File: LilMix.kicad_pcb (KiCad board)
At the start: 2 copper layers, 47 parts, among them J1_L1 PJ301BM, J1_R1 PJ301BM, J2_L1 PJ301BM, J2_R1 PJ301BM, J3 JACK-STEREO-MINI, J4 PJ301BM, J5 PJ301BM, J6 JACK-STEREO-MINI, U1 TL074, U2 NE5532

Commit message: Very rough component placement
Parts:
- moved U1 96.0 mm to (318.4, 112.0), turned to 90 degrees
- moved R1 90.6 mm to (272.6, 121.2)
- moved C1 89.8 mm to (281.6, 122.7)
- moved R15 89.8 mm to (276.8, 122.0)
- moved C10 89.2 mm to (259.6, 122.2)
- moved C9 89.2 mm to (264.4, 122.6)
- moved D1 89.2 mm to (265.9, 119.4)
- moved D2 89.2 mm to (260.1, 119.1)
- moved U2 89.2 mm to (253.0, 120.6)
- moved R5 86.8 mm to (301.4, 111.2)
- moved C3 83.6 mm to (306.2, 110.6)
- moved C4 78.6 mm to (306.8, 121.2)
- moved R17 78.6 mm to (306.9, 116.9)
- moved R9 78.3 mm to (286.1, 122.4)
- moved R6 76.4 mm to (302.6, 117.2)
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
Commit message: Updated rough placement and circuit updates
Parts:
- added JP2: 2x4 Socket, 4ms-footprints:Socket_2x4_2.54mm_TH, F.Cu at (98.9, 145.1)
- added JP3: 2x4 Socket, 4ms-footprints:Socket_2x4_2.54mm_TH, F.Cu at (115.7, 78.9)
- added RV5: 100k, 4ms-footprints:Audio_Mod_Header_1x03, B.Cu at (176.0, 24.9)
- added RV6: 100k, 4ms-footprints:Audio_Mod_Header_1x03, B.Cu at (203.6, 50.6)
- C1, C10, C2, C3, C4, C5, C6, C7, C8, C9, D1, D2, R1, R10, R11, R12, R13, R14, R15, R16, R17, R18, R19, R2, R20, R4, R5, R9, U1, U2: moved to B.Cu
- JP1: value EURO_HEADER_10pin -> 2x8 Power; moved to B.Cu
- R3, R6: value 100k -> 47k; moved to B.Cu
- R7, R8: value 39k -> 100k; moved to B.Cu
- moved J6 232.9 mm to (102.2, 94.5), turned to 270 degrees
- moved RV4 225.0 mm to (99.9, 77.3)
- moved U1 204.2 mm to (115.0, 94.2), turned to 270 degrees
- moved R9 189.0 mm to (103.5, 73.5), turned to 180 degrees
- moved J5 186.8 mm to (146.9, 94.5), turned to 270 degrees
- moved C4 184.6 mm to (123.4, 100.6)
- moved C3 183.1 mm to (124.6, 87.6)
- moved R10 180.1 mm to (97.8, 91.5), turned to 180 degrees
- moved R13 176.9 mm to (120.1, 87.6)
- moved R17 176.8 mm to (131.1, 98.9), turned to 270 degrees
- moved C5 171.3 mm to (114.4, 100.7)
- moved R14 164.9 mm to (128.7, 94.0), turned to 270 degrees
- moved RV1 162.8 mm to (124.0, 77.3)
- moved R7 162.8 mm to (162.3, 19.1)
- moved RV2 159.2 mm to (141.4, 77.3)
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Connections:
- J1_L1 pad 1: GND -> GND_B
- J1_R1 pad 1: GND -> GND_B
- J1_R1 pad 3: Net-(J1_R1-Pad3) -> J1_R_B
- J2_L1 pad 1: GND -> GND_B
- J2_R1 pad 1: GND -> GND_B
- J2_R1 pad 3: Net-(J2_R1-Pad3) -> J2_R_B
- J3 pad 1: J3_INSERT -> J3_L_B
- J3 pad 2: GND -> GND_B
- J3 pad 3: Net-(J3-Pad3) -> J3_R_B
- JP1 pad 1: Net-(JP1-Pad1) -> Net-(D1-Pad2)
- JP1 pad 9: Net-(JP1-Pad9) -> Net-(D2-Pad1)
- R11 pad 2: L_INV -> Net-(R11-Pad2)
- R12 pad 2: R_INV -> Net-(R12-Pad2)
- RV1 pad 3: J1_INSERT -> J1_L_A
- RV1 pad 6: J2_INSERT -> J2_L_A
- RV2 pad 3: J3_INSERT -> J3_L_A
- RV2 pad 6: Net-(J1_R1-Pad3) -> J1_R_A
- RV3 pad 3: Net-(J2_R1-Pad3) -> J2_R_A
- RV3 pad 6: Net-(J3-Pad3) -> J3_R_A
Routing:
- added copper zone on B.Cu, net GND
- added copper zone on F.Cu, net GND
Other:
- board outline added: 46.6 x 1.9 mm
- board text added: "Front 4.8 x 8.1 cm"
- board text added: "Top Drills 2.1 x 8.1 cm"

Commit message: Rought placement complete
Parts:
- J1_L1, J1_R1, J2_L1, J2_R1, J4, J5: value PJ301BM -> MONO
- J3, J6: value JACK-STEREO-MINI -> STEREO
- moved R11 91.2 mm to (115.2, 101.7), turned to 270 degrees
- moved R15 88.8 mm to (118.0, 101.7), turned to 90 degrees
- moved C6 86.2 mm to (111.7, 85.6), turned to 90 degrees
- moved R7 85.7 mm to (108.3, 85.6), turned to 90 degrees
- moved C9 85.1 mm to (120.6, 101.7), turned to 270 degrees
- moved R8 82.0 mm to (118.6, 85.5), turned to 270 degrees
- moved C7 81.7 mm to (122.3, 85.5), turned to 270 degrees
- moved R12 68.0 mm to (151.2, 99.2), turned to 90 degrees
- moved RV5 67.8 mm to (146.9, 86.1), turned to 90 degrees
- moved RV6 64.5 mm to (155.1, 93.2)
- moved C10 62.5 mm to (142.6, 94.7), turned to 90 degrees
- moved R16 61.5 mm to (154.8, 99.3), turned to 270 degrees
- moved R13 6.19 mm to (125.9, 85.5), turned to 90 degrees
- moved C3 5.23 mm to (129.4, 85.6), turned to 270 degrees
- moved R19 3.96 mm to (105.0, 85.6), turned to 90 degrees
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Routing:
- removed copper zone on B.Cu, net GND
- removed copper zone on F.Cu, net GND

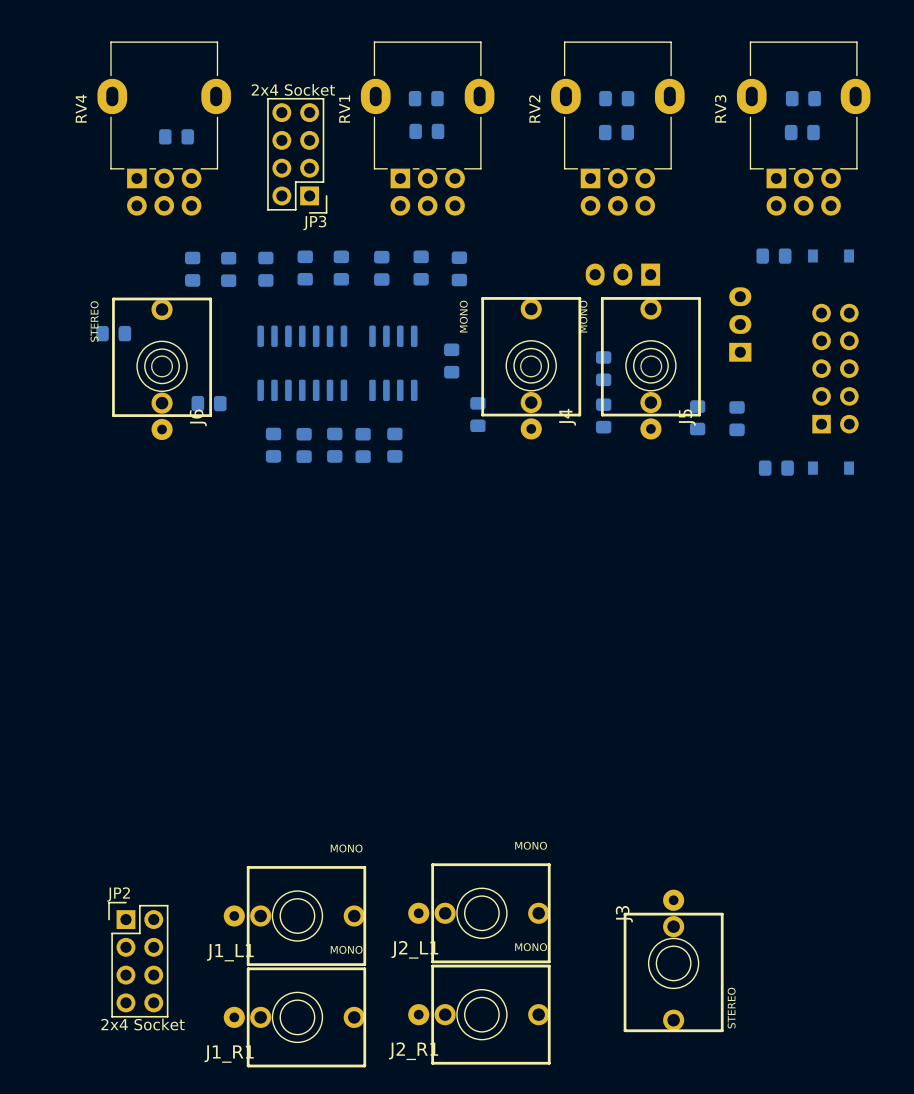
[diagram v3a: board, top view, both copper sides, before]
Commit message: Updated project traces. Added board cuts
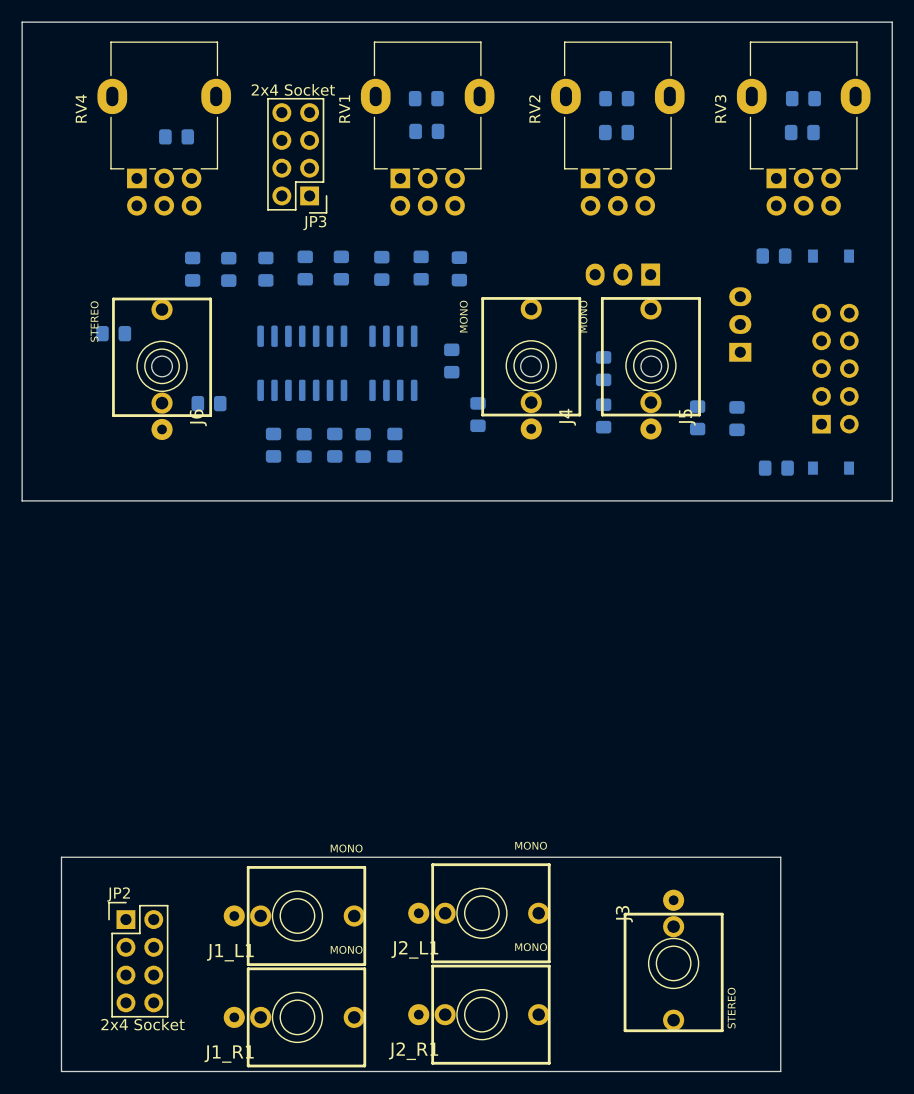
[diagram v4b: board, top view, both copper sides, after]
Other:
- board size 46.6 x 1.9 mm -> 79.6 x 96 mm
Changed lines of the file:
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@@
   (general
     (thickness 1.6)
-    (drawings 11)
+    (drawings 19)
     (tracks 0)
     (zones 0)
@@
   (setup
     (last_trace_width 0.25)
+    (user_trace_width 0.3)
+    (user_trace_width 0.4)
+    (user_trace_width 0.5)
+    (user_trace_width 0.75)
     (trace_clearance 0.2)
     (zone_clearance 0.508)
@@
     )
   )
+  (gr_line (start 169 106.8) (end 89.4 106.8) (layer Edge.Cuts) (width 0.05))
+  (gr_line (start 89.4 63) (end 89.4 106.8) (layer Edge.Cuts) (width 0.05))
+  (gr_line (start 169 63) (end 89.4 63) (layer Edge.Cuts) (width 0.05))
+  (gr_line (start 169 106.8) (end 169 63) (layer Edge.Cuts) (width 0.05))
+  (gr_line (start 93 139.4) (end 93 159) (layer Edge.Cuts) (width 0.05))
+  (gr_line (start 158.8 139.4) (end 93 139.4) (layer Edge.Cuts) (width 0.05))
+  (gr_line (start 158.8 159) (end 158.8 139.4) (layer Edge.Cuts) (width 0.05))
+  (gr_line (start 93 159) (end 158.8 159) (layer Edge.Cuts) (width 0.05))
   (gr_circle (center 146.956602 94.5) (end 147.756602 94) (layer Edge.Cuts) (width 0.05))
   (gr_circle (center 135.956602 94.5) (end 136.756602 94) (layer Edge.Cuts) (width 0.05))

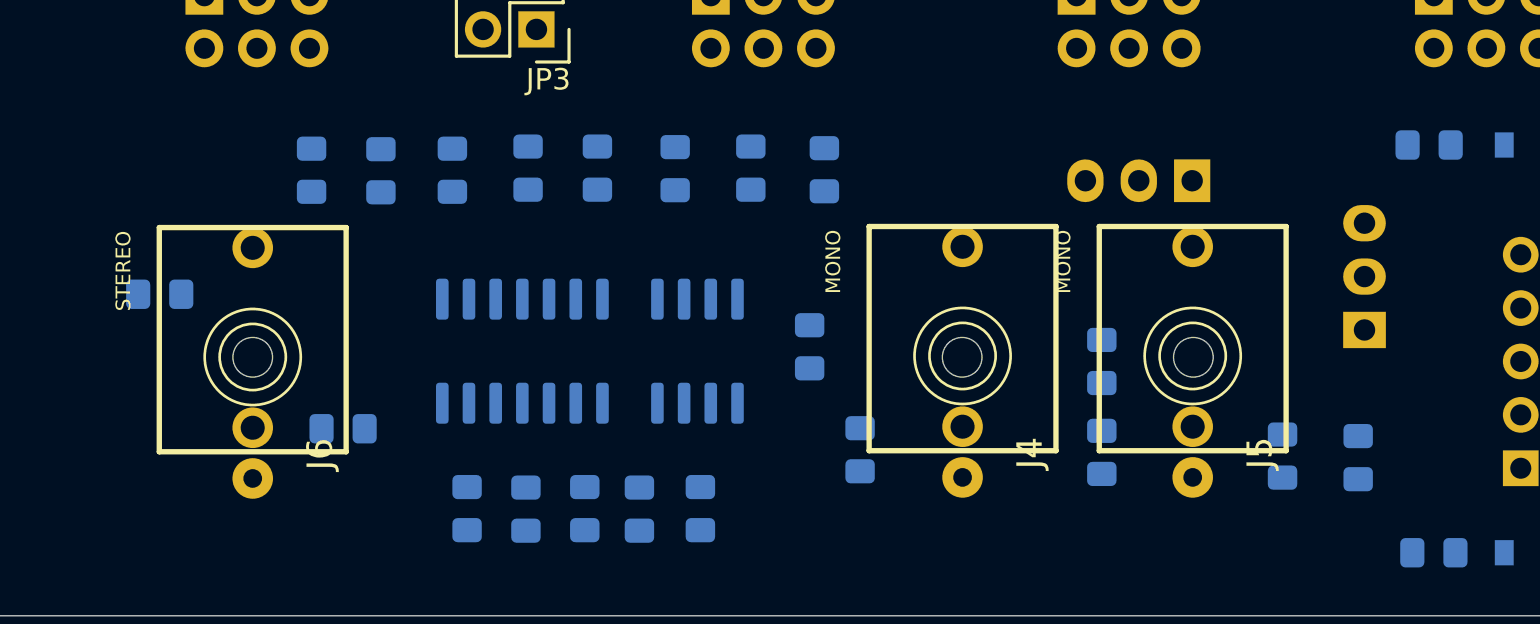
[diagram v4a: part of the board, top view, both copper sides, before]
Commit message: Added power sockets for other modules
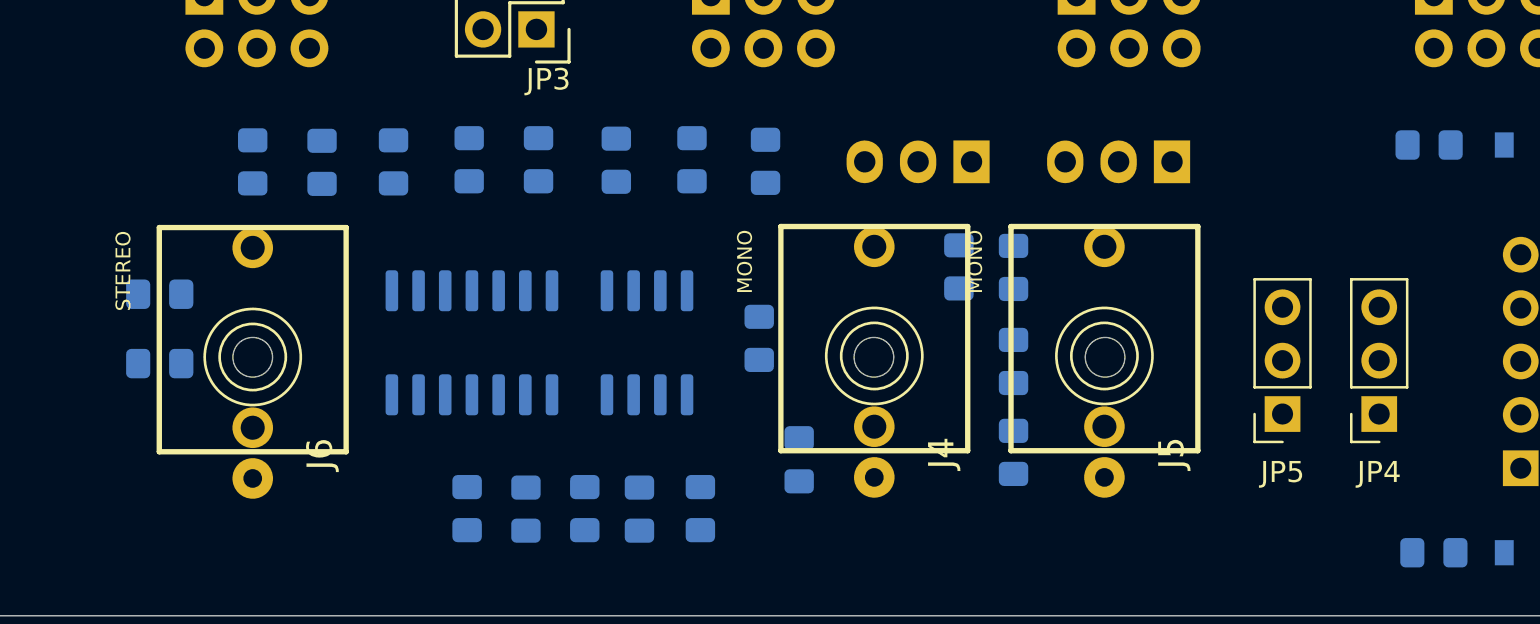
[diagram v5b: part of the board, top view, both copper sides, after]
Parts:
- added JP4: Conn_01x03, Connector_PinSocket_2.54mm:PinSocket_1x03_P2.54mm_Vertical, F.Cu at (155.8, 97.2)
- added JP5: Conn_01x03, Connector_PinSocket_2.54mm:PinSocket_1x03_P2.54mm_Vertical, F.Cu at (151.2, 97.2)
- moved R16 21.1 mm to (135.8, 90.2), turned to 90 degrees
- moved R12 15.6 mm to (138.4, 90.2)
- moved RV6 12.2 mm to (145.9, 85.2), turned to 90 degrees
- moved RV5 10.5 mm to (136.4, 85.2)
- moved R20 9.26 mm to (97.8, 94.8)
- moved J5 4.20 mm to (142.7, 94.5)
- moved C10 4.20 mm to (138.4, 94.7)
- moved J4 4.20 mm to (131.8, 94.5)
- moved R18 4.20 mm to (138.4, 99.0)
- moved R17 2.94 mm to (128.2, 99.4)
- moved C3 2.83 mm to (126.6, 85.2)
- moved R13 2.83 mm to (123.1, 85.1)
- moved C7 2.83 mm to (119.5, 85.1)
- moved C8 2.83 mm to (112.5, 85.1)
- moved R7 2.83 mm to (105.5, 85.2)
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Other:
- outline, holes or cut-outs redrawn

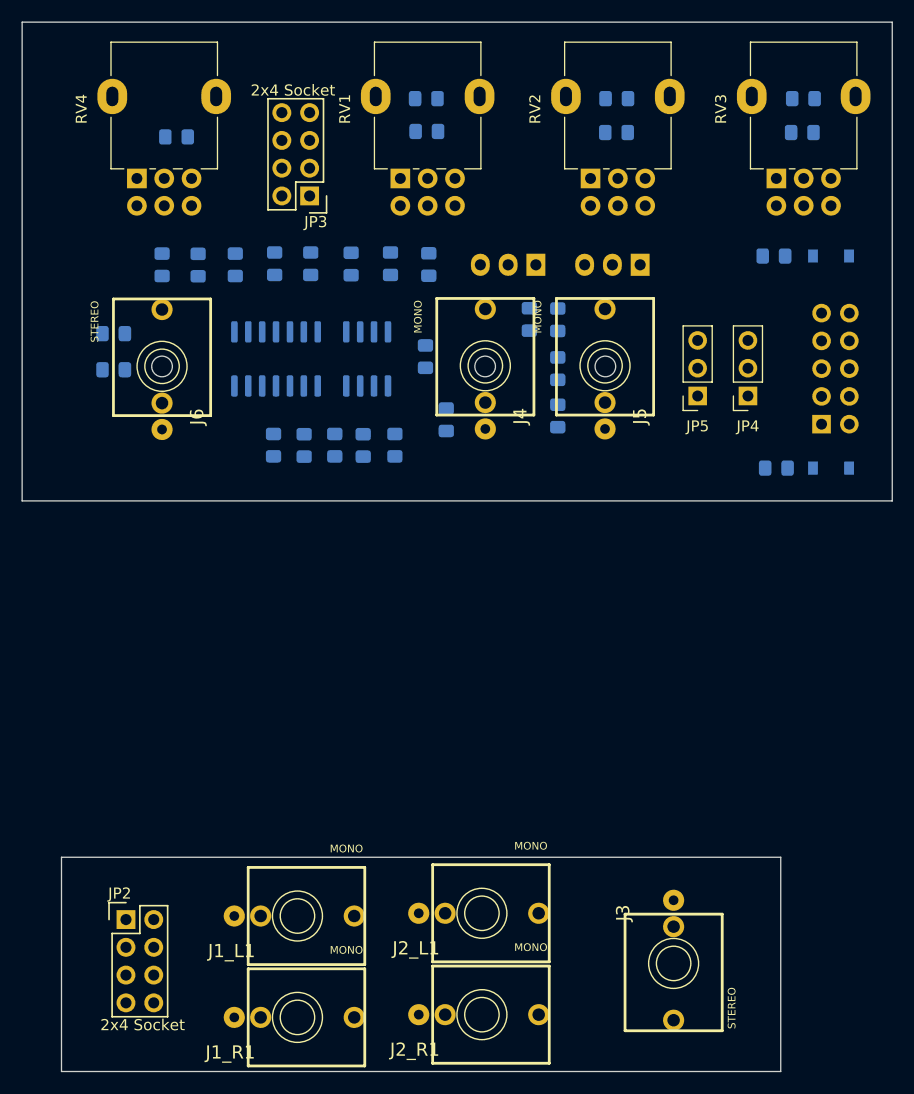
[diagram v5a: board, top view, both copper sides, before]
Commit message: Updated footprint of stereo jacks
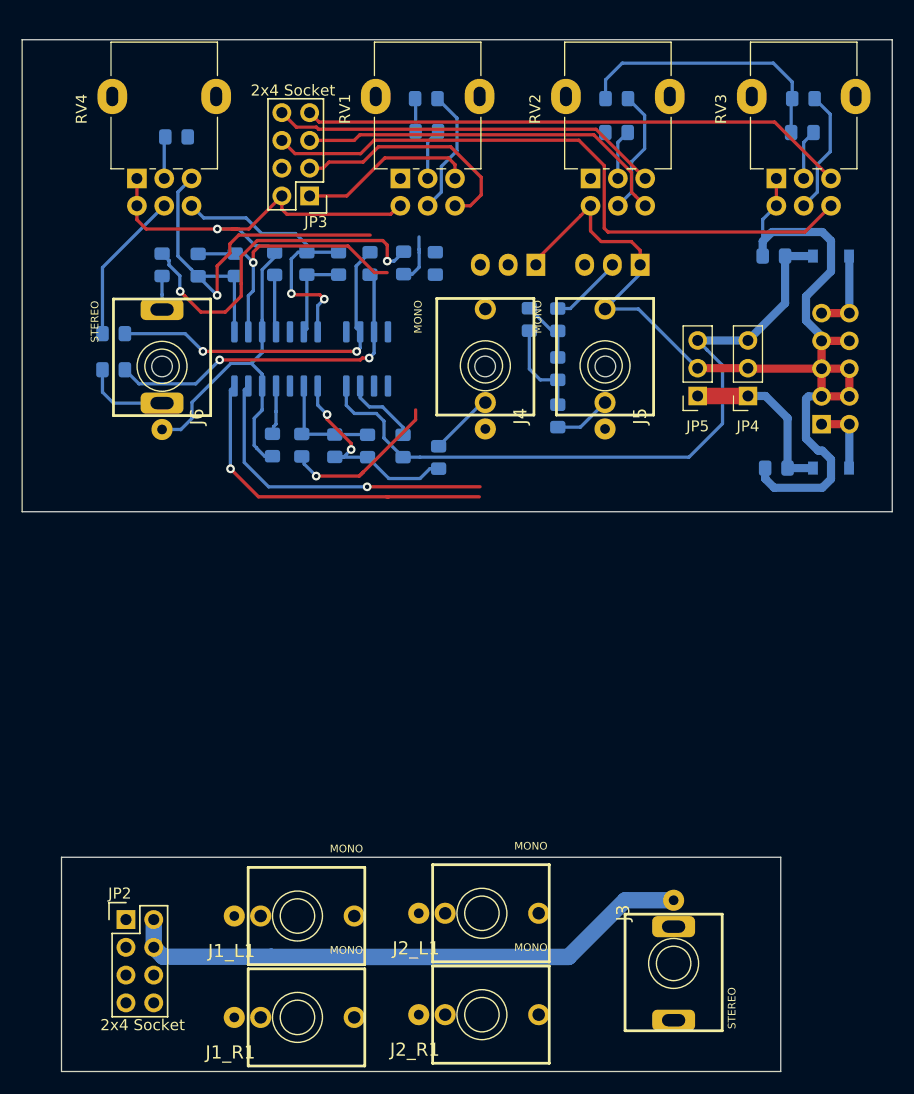
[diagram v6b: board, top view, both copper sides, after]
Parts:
- J3, J6: footprint 4ms-footprints:PJ301M-12 -> Eurocad:STPX-3501-3C-1
- moved C4 17.0 mm to (127.2, 85.1), turned to 90 degrees
- moved C3 16.8 mm to (124.2, 101.8)
- moved R14 9.92 mm to (121.2, 85.1), turned to 90 degrees
- moved R17 3.52 mm to (127.5, 102.8)
- moved R15 3.00 mm to (121.0, 101.8)
- moved C9 2.60 mm to (118.0, 101.8), turned to 90 degrees
- moved R13 1.20 mm to (124.3, 85.0), turned to 270 degrees
- moved C7 1.15 mm to (118.3, 85.1)
- moved R8 0.35 mm to (115.5, 85.1)
- moved R11 0.22 mm to (115.0, 101.7)
- moved C5 0.10 mm to (112.3, 101.7)
- turned U2 to 90 degrees
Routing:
- net GND: track 0.00 -> 181.0 mm, vias 0 -> 1
- net -12V: track 0.00 -> 69.6 mm
- net J3_R_A: track 0.00 -> 59.1 mm
- net GND_B: track 0.00 -> 52.6 mm
- net J2_R_A: track 0.00 -> 50.2 mm
- net Net-(C10-Pad1): track 0.00 -> 40.5 mm, vias 0 -> 1
- net L_INV: track 0.00 -> 39.6 mm, vias 0 -> 1
- net J3_L_A: track 0.00 -> 35.7 mm
- net Net-(C10-Pad2): track 0.00 -> 35.5 mm, vias 0 -> 1
- net J1_R_A: track 0.00 -> 34.7 mm
- net Net-(C7-Pad2): track 0.00 -> 33.1 mm
- net Net-(R13-Pad1): track 0.00 -> 32.2 mm, vias 0 -> 2
- net Net-(R14-Pad1): track 0.00 -> 31.8 mm, vias 0 -> 2
- net Net-(R10-Pad1): track 0.00 -> 31.8 mm, vias 0 -> 2
- net Net-(C6-Pad2): track 0.00 -> 29.4 mm, vias 0 -> 1
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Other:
- board size 79.6 x 96 mm -> 79.6 x 94.4 mm
